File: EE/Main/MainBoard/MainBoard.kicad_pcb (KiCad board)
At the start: 2 copper layers, 185.6 x 109.5 mm, 18 parts, among them J1 Conn_02x13_Odd_Even

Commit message: First pass exterior
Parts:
- moved H5 4.29 mm to (131.1, 134.8)
- moved H6 4.29 mm to (155.1, 134.8)
- moved H1 4.29 mm to (96.1, 68.7)
- moved H10 4.29 mm to (190.5, 69.3)
- moved H11 4.29 mm to (155.6, 54.8)
- moved H2 4.29 mm to (79.1, 85.7)
- moved H3 4.29 mm to (79.1, 103.3)
- moved H4 4.29 mm to (96.1, 120.3)
- moved H7 4.29 mm to (190.5, 120.9)
- moved H8 4.29 mm to (207.5, 104.0)
- moved H9 4.29 mm to (207.5, 86.3)
- moved J4 4.29 mm to (199.1, 77.8)
- moved J4 4.29 mm to (199.0, 112.5)
- moved locked 4.29 mm to (131.6, 54.8)
- moved J1 4.29 mm to (87.6, 77.1)
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- renumbered H2 to H10, H1 to H11, H1 to H3, H2 to H4, H1 to H5, H2 to H6, H1 to H7, H2 to H8, H1 to H9, J1 to J2, J1 to J3, J1 to J4, J1 to J5, H2 to locked
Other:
- board size 185.6 x 109.5 mm -> 185 x 89.6 mm

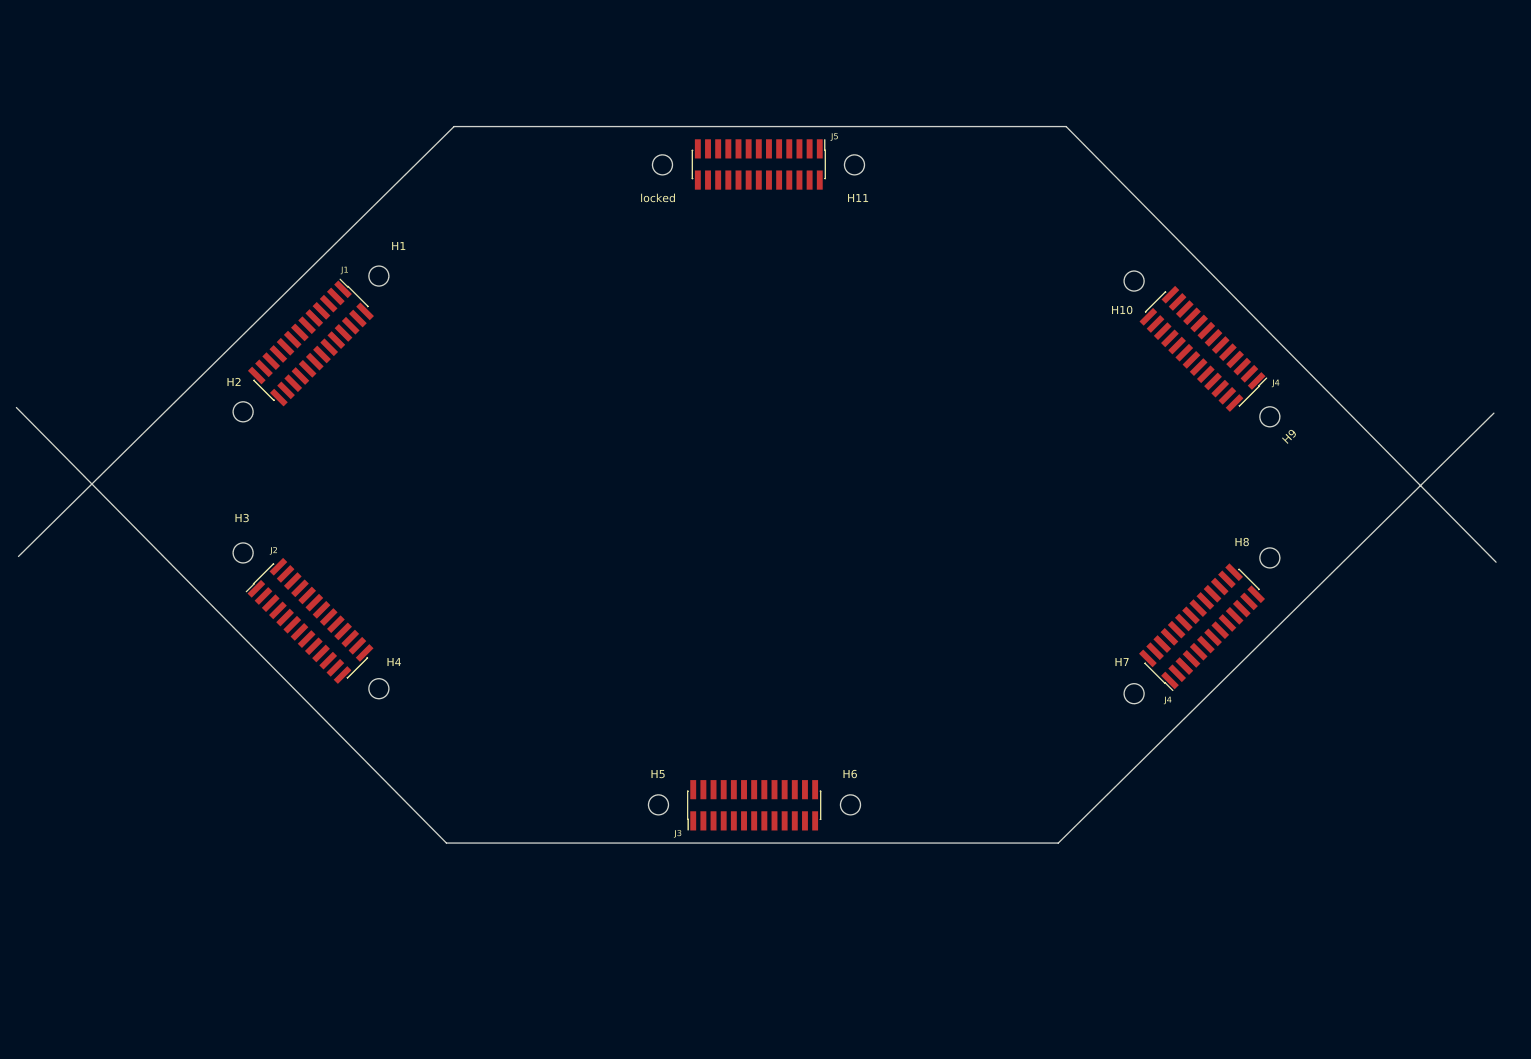
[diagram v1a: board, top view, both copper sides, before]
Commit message: WIP - Moving Sensor to IO Expander
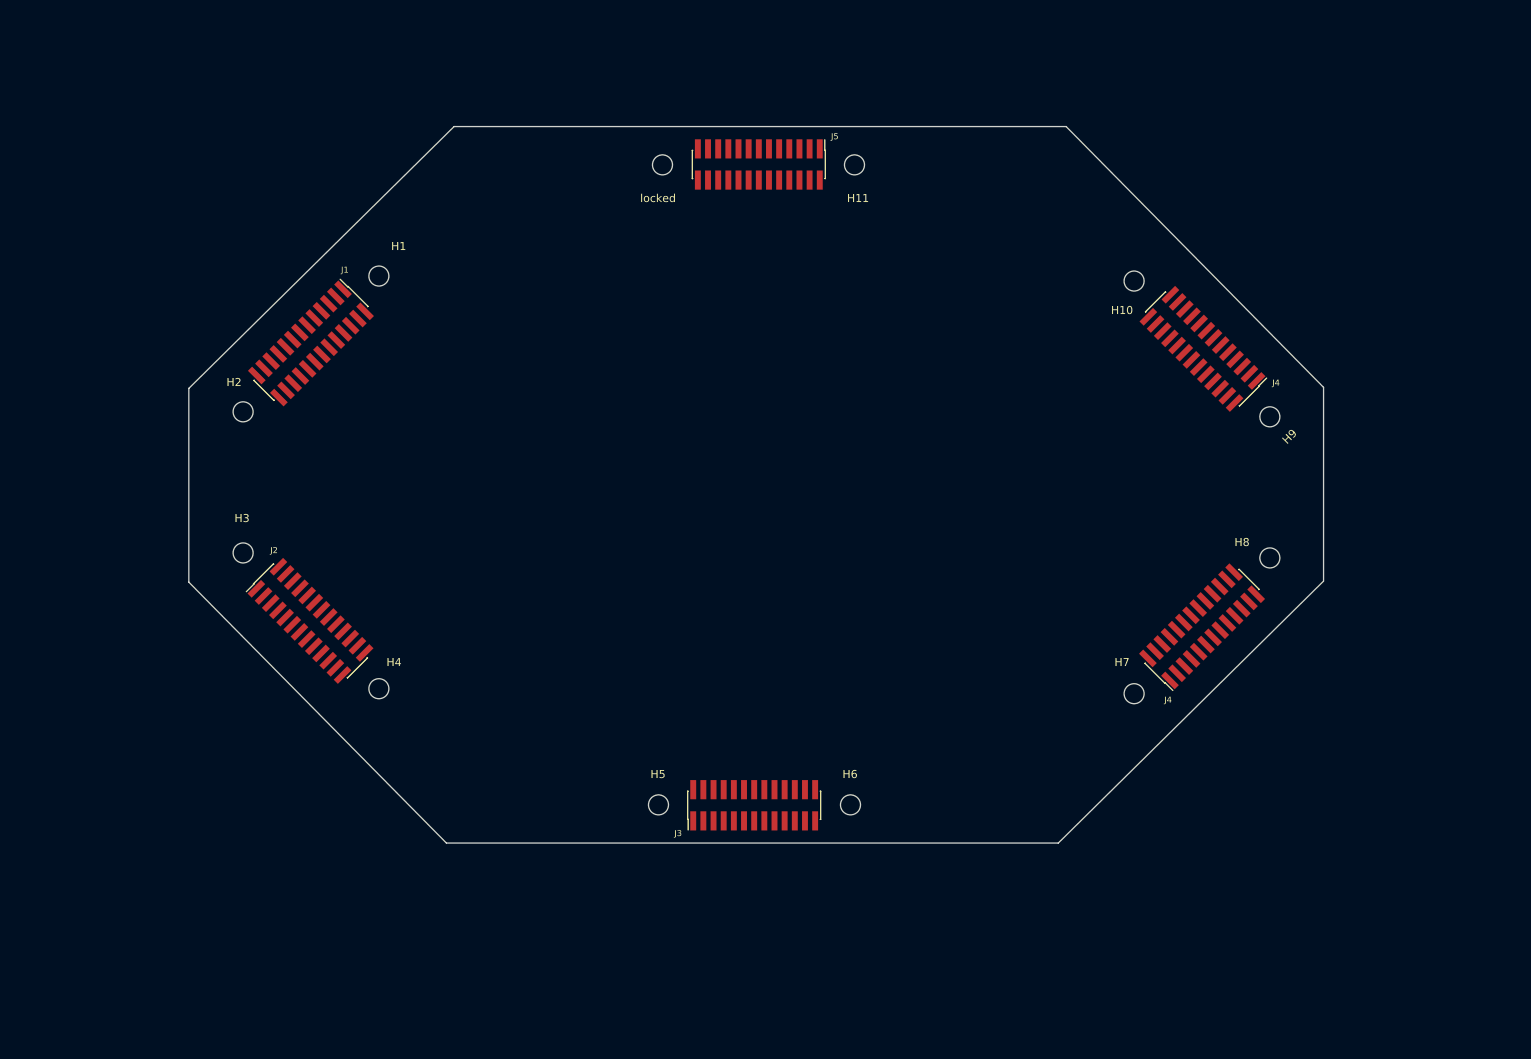
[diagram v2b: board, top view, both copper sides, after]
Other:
- board size 185 x 89.6 mm -> 141.8 x 89.6 mm
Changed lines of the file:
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@@
     (pad "" np_thru_hole circle locked (at 0 0 135) (size 2.5 2.5) (drill 2.5) (layers *.Cu *.Mask))
   )
-  (gr_line (start 51.055 103.77) (end 105.505 50.03) (layer "Edge.Cuts") (width 0.1))
+  (gr_line (start 72.35 82.76) (end 105.505 50.03) (layer "Edge.Cuts") (width 0.1))
+  (gr_line (start 72.35 82.76) (end 72.35 106.98) (layer "Edge.Cuts") (width 0.1))
   (gr_line (start 105.505 50.03) (end 182.015 50.03) (layer "Edge.Cuts") (width 0.1))
-  (gr_line (start 235.485 85.85) (end 181.035 139.59) (layer "Edge.Cuts") (width 0.1))
-  (gr_line (start 50.795 85.15) (end 104.545 139.59) (layer "Edge.Cuts") (width 0.1))
-  (gr_line (start 182.015 50.03) (end 235.755 104.48) (layer "Edge.Cuts") (width 0.1))
+  (gr_line (start 214.19 106.85) (end 181.035 139.59) (layer "Edge.Cuts") (width 0.1))
+  (gr_line (start 214.19 82.63) (end 214.19 106.85) (layer "Edge.Cuts") (width 0.1))
+  (gr_line (start 72.35 106.98) (end 104.545 139.59) (layer "Edge.Cuts") (width 0.1))
+  (gr_line (start 182.015 50.03) (end 214.19 82.63) (layer "Edge.Cuts") (width 0.1))
   (gr_line (start 181.035 139.59) (end 104.545 139.59) (layer "Edge.Cuts") (width 0.1))
   (gr_line (start 50.497105 93.819351) (end 77.367163 93.819351) (layer "B.Fab") (width 0.1))

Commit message: Updated layout, and placement for main board
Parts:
- removed the J4 at (199.1, 77.8)
- removed the J4 at (199.0, 112.5)
- removed locked: MountingHole, MountingHole:MountingHole_2.5mm
- added C1: 0.1u, Capacitor_SMD:C_0402_1005Metric, F.Cu at (164.0, 114.0)
- added C2: 4.7u, Capacitor_SMD:C_0603_1608Metric, F.Cu at (122.0, 114.4)
- added C3: 4.7u, Capacitor_SMD:C_0603_1608Metric, F.Cu at (126.3, 110.8)
- added C4: 4.7u, Capacitor_SMD:C_0603_1608Metric, F.Cu at (110.4, 129.0)
- added C5: 4.7u, Capacitor_SMD:C_0603_1608Metric, F.Cu at (110.4, 126.5)
- added C6: 4.7u, Capacitor_SMD:C_0603_1608Metric, F.Cu at (115.6, 122.0)
- added H12: MountingHole, MountingHole:MountingHole_2.5mm, F.Cu at (79.1, 85.7)
- added H13: MountingHole, MountingHole:MountingHole_2.5mm, F.Cu at (172.9, 154.2)
- added H14: MountingHole, MountingHole:MountingHole_2.5mm, F.Cu at (166.3, 154.2)
- added H15: MountingHole, MountingHole:MountingHole_2.5mm, F.Cu at (166.3, 160.7)
- added H16: MountingHole, MountingHole:MountingHole_2.5mm, F.Cu at (172.9, 160.7)
- added J4: Conn_01x04_Male, Connector_PinSocket_2.54mm:PinSocket_1x04_P2.54mm_Vertical, F.Cu at (199.2, 82.6)
- added J6: Conn_01x04_Male, Connector_PinSocket_2.54mm:PinSocket_1x04_P2.54mm_Vertical, F.Cu at (92.4, 77.0)
- added J7: TAG_CONNECT, Connector:Tag-Connect_TC2030-IDC-FP_2x03_P1.27mm_Vertical, F.Cu at (158.2, 110.6)
- added P1: USB_C_Plug_USB2.0, Connector_USB:USB_C_Receptacle_GCT_USB4085, F.Cu at (113.0, 155.8)
- added Q1: 2N7002NXAKR, Package_TO_SOT_SMD:SC-59, F.Cu at (141.9, 71.1)
- added Q2: 2N7002NXAKR, Package_TO_SOT_SMD:SC-59, F.Cu at (170.9, 118.0)
- added Q3: 2N7002NXAKR, Package_TO_SOT_SMD:SC-59, F.Cu at (137.1, 71.1)
- added Q4: 2N7002NXAKR, Package_TO_SOT_SMD:SC-59, F.Cu at (176.0, 118.0)
- added R1: 4.7k, Resistor_SMD:R_0402_1005Metric, F.Cu at (164.0, 112.1)
- added R10: 560, Resistor_SMD:R_0402_1005Metric, F.Cu at (177.7, 106.3)
- added R11: 560, Resistor_SMD:R_0402_1005Metric, F.Cu at (169.9, 111.0)
- added R12: 560, Resistor_SMD:R_0402_1005Metric, F.Cu at (148.7, 69.8)
- added R13: 560, Resistor_SMD:R_0402_1005Metric, F.Cu at (174.8, 106.3)
- added R14: 20k, Resistor_SMD:R_0402_1005Metric, F.Cu at (113.9, 126.2)
- added R15: 2k, Resistor_SMD:R_0402_1005Metric, F.Cu at (121.5, 118.6)
- added R16: 100k, Resistor_SMD:R_0402_1005Metric, F.Cu at (121.5, 116.6)
- added R2: 4.7k, Resistor_SMD:R_0402_1005Metric, F.Cu at (169.2, 106.8)
- added R3: 10k, Resistor_SMD:R_0402_1005Metric, F.Cu at (145.8, 71.8)
- added R4: 10k, Resistor_SMD:R_0402_1005Metric, F.Cu at (151.7, 69.8)
- added R5: 10k, Resistor_SMD:R_0402_1005Metric, F.Cu at (169.9, 113.0)
- added R6: 10k, Resistor_SMD:R_0402_1005Metric, F.Cu at (174.8, 108.3)
- added R7: 560, Resistor_SMD:R_0402_1005Metric, F.Cu at (172.8, 111.0)
- added R8: 560, Resistor_SMD:R_0402_1005Metric, F.Cu at (148.7, 71.8)
- added R9: 560, Resistor_SMD:R_0402_1005Metric, F.Cu at (145.8, 69.8)
- added U1: STM32C011F4U6TR, Package_DFN_QFN:UQFN-20_3x3mm_P0.4mm, F.Cu at (165.2, 108.5)
- added U2: DA04-11EWA, Display_7Segment:DA04-11SURKWA, F.Cu at (163.2, 100.3)
- added U3: DA04-11GWA, Display_7Segment:DA04-11CGKWA, F.Cu at (107.2, 100.3)
- added U4: MCP73832-2-OT, Package_TO_SOT_SMD:SOT-23-5, F.Cu at (111.0, 123.0)
- added U5: TPS62172DSG, Package_SON:WSON-8-1EP_2x2mm_P0.5mm_EP0.9x1.6mm_ThermalVias, F.Cu at (117.8, 108.2)
- J1, J2, J3, J5: value Conn_02x13_Odd_Even -> Conn_01x04_Male; footprint Connector_PinHeader_1.27mm:PinHeader_2x13_P1.27mm_Vertical_SMD -> Connector_PinSocket_2.54mm:PinSocket_1x04_P2.54mm_Vertical
- moved H9 82.2 mm to (131.5, 54.8), turned to -90 degrees
- moved H3 82.2 mm to (155.1, 134.8), turned to 90 degrees
- moved H5 61.1 mm to (190.5, 120.9), turned to 135 degrees
- moved H11 61.0 mm to (96.1, 68.7), turned to -45 degrees
- moved H6 60.9 mm to (207.5, 104.0), turned to 135 degrees
- moved J3 55.9 mm to (194.3, 112.6), turned to 135 degrees
- moved J2 55.6 mm to (139.6, 131.6), turned to 90 degrees
- moved H7 51.6 mm to (190.5, 69.3), turned to -135 degrees
- moved H1 38.6 mm to (79.1, 103.3), turned to 45 degrees
- moved H2 38.5 mm to (96.1, 120.3), turned to 45 degrees
- moved H10 37.9 mm to (155.6, 54.8), turned to -90 degrees
- moved H4 37.9 mm to (131.1, 134.8), turned to 90 degrees
- moved J1 29.9 mm to (87.4, 107.1), turned to 45 degrees
- moved H8 17.6 mm to (207.5, 86.3), turned to -135 degrees
- moved J5 4.76 mm to (147.0, 58.0)
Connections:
- J1 pad 1: (no net) -> VCC
- J1 pad 2: (no net) -> /SCL
- J1 pad 3: (no net) -> /SDA
- J1 pad 4: (no net) -> GND
- J2 pad 1: (no net) -> VCC
- J2 pad 2: (no net) -> /SCL
- J2 pad 3: (no net) -> /SDA
- J2 pad 4: (no net) -> GND
- J3 pad 1: (no net) -> VCC
- J3 pad 2: (no net) -> /SCL
- J3 pad 3: (no net) -> /SDA
- J3 pad 4: (no net) -> GND
- J5 pad 1: (no net) -> VCC
- J5 pad 2: (no net) -> /SCL
- J5 pad 3: (no net) -> /SDA
- J5 pad 4: (no net) -> GND

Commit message: Routed PCB, Need SCL/SDA still
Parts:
- added D1: LED, LED_SMD:LED_0603_1608Metric, F.Cu at (113.6, 121.2)
- added J8: Conn_01x02_Male, Connector_JST:JST_PH_B2B-PH-K_1x02_P2.00mm_Vertical, F.Cu at (144.5, 109.3)
- added L1: 2.2u, Inductor_SMD:L_0805_2012Metric, F.Cu at (177.7, 127.7)
- added R17: 0, Resistor_SMD:R_0402_1005Metric, F.Cu at (146.0, 112.2)
- added R18: 0, Resistor_SMD:R_0402_1005Metric, F.Cu at (140.8, 112.2)
- added R19: 0, Resistor_SMD:R_0402_1005Metric, F.Cu at (144.2, 112.7)
- added R20: 0, Resistor_SMD:R_0402_1005Metric, F.Cu at (142.5, 112.7)
- added SW1: EG1206A, Library:EG1206A_EWI, F.Cu at (170.0, 135.8)
- moved R13 71.0 mm to (107.2, 84.3), turned to -90 degrees
- moved R10 70.7 mm to (107.0, 106.0)
- moved C5 68.6 mm to (178.9, 130.9), turned to -90 degrees
- moved R7 68.4 mm to (109.8, 84.5), turned to -90 degrees
- moved C1 68.4 mm to (108.7, 73.8), turned to -135 degrees
- moved R1 65.8 mm to (111.3, 72.6), turned to -45 degrees
- moved R2 65.7 mm to (112.8, 73.3), turned to -135 degrees
- moved U1 63.7 mm to (110.5, 75.8), turned to -45 degrees
- moved R11 63.1 mm to (107.2, 103.3)
- moved C6 62.5 mm to (177.4, 130.9), turned to -90 degrees
- moved C4 61.0 mm to (171.4, 127.7), turned to 180 degrees
- moved Q4 60.7 mm to (116.8, 105.0)
- moved U5 60.2 mm to (174.8, 127.8)
- moved Q2 60.1 mm to (112.2, 105.0)
- moved R6 56.8 mm to (118.0, 108.0), turned to -90 degrees
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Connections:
- U1 pad 10: /Display/F_EN -> /Display/G_EN
- U1 pad 11: /Display/G_EN -> /Display/A_EN
- U1 pad 12: /Display/D1_R_EN -> /Display/F_EN
- U1 pad 13: /Display/D2_R_EN -> /Display/B_EN
- U1 pad 14: /Display/D1_G_EN -> /Display/D2_R_EN
- U1 pad 15: /Display/D2_G_EN -> /Display/D1_R_EN
- U1 pad 5: /Display/A_EN -> /Display/D2_G_EN
- U1 pad 6: /Display/B_EN -> /Display/D1_G_EN
- U1 pad 7: /Display/C_EN -> /Display/D_EN
- U1 pad 8: /Display/D_EN -> /Display/E_EN
- U1 pad 9: /Display/E_EN -> /Display/C_EN
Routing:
- net /Display/D1_R_EN: track 0.00 -> 118.9 mm
- net /Display/D2_R_EN: track 0.00 -> 105.3 mm
- net /Power/VBAT: track 0.00 -> 87.1 mm
- net /Display/C: track 0.00 -> 83.9 mm
- net /Display/G: track 0.00 -> 83.1 mm
- net /Display/E: track 0.00 -> 80.3 mm
- net /Display/A: track 0.00 -> 78.3 mm
- net /Display/D: track 0.00 -> 77.7 mm
- net /Display/F: track 0.00 -> 72.7 mm
- net /Display/B: track 0.00 -> 65.9 mm
- net /Display/D2_G_EN: track 0.00 -> 62.2 mm
- net /Display/D1_G_EN: track 0.00 -> 51.9 mm
- net /Display/D_EN: track 0.00 -> 39.3 mm
- net GND: track 0.00 -> 36.0 mm, vias 0 -> 22
- net /Display/E_EN: track 0.00 -> 34.5 mm
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- added copper zone on B.Cu, net GND
- added copper zone on F.Cu, net VCC
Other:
- board size 141.8 x 89.6 mm -> 135.8 x 87.5 mm

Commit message: First pass Finalized Layout. Pending Sensing board changes.
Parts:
- removed H13, H14, H15, H16: MountingHole, MountingHole:MountingHole_2.5mm
- moved C5 0.60 mm to (178.3, 130.9)
- moved C6 0.60 mm to (176.8, 130.9)
- moved SW1 0.10 mm to (170.0, 135.9)
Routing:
- net /SDA: track 1.76 -> 293.3 mm, vias 0 -> 3
- net /SCL: track 2.58 -> 277.4 mm, vias 0 -> 8
- net VCC: track 13.0 -> 20.8 mm
- net GND: track 36.0 -> 38.5 mm
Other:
- board text added: "PRT-13851"
